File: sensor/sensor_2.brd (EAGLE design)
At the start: 40.1 x 55.9 mm, 29 parts, among them IC1 INA116U, IC3 LT6230LT6010(MOD12.2013), T1 BC849SMD, T2 BC849SMD

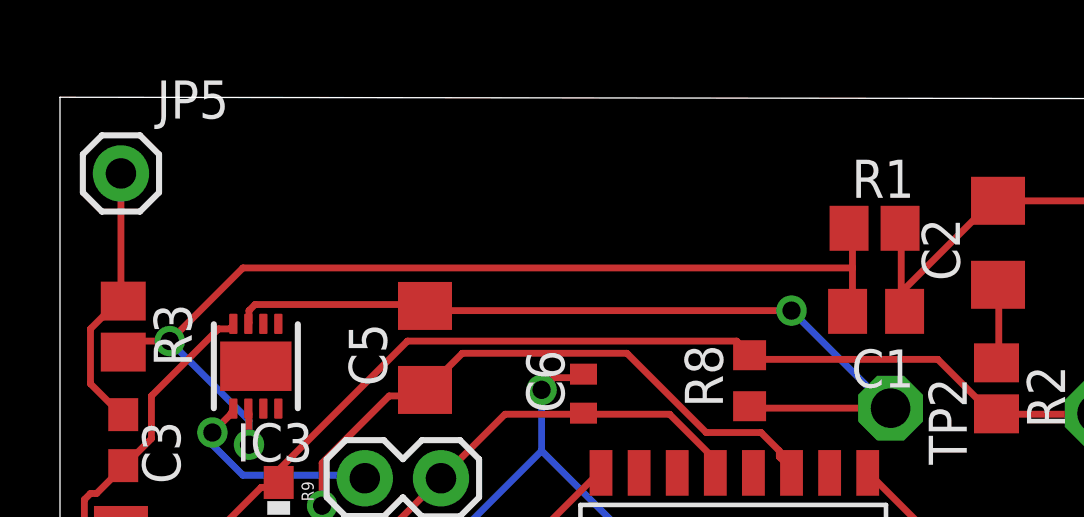
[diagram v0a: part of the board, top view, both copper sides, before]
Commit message: IC3 had green lines that were part of the via layer. Those were removed. There was also a missing trace from PIN2 of the IC3 part. That was restored. Small tweaks were made. Sensor board seems to be done. Next is to export it into the appropriate files for the fre DFM check by Advance Circuits. After that, the board will be submitted to OHSpark.
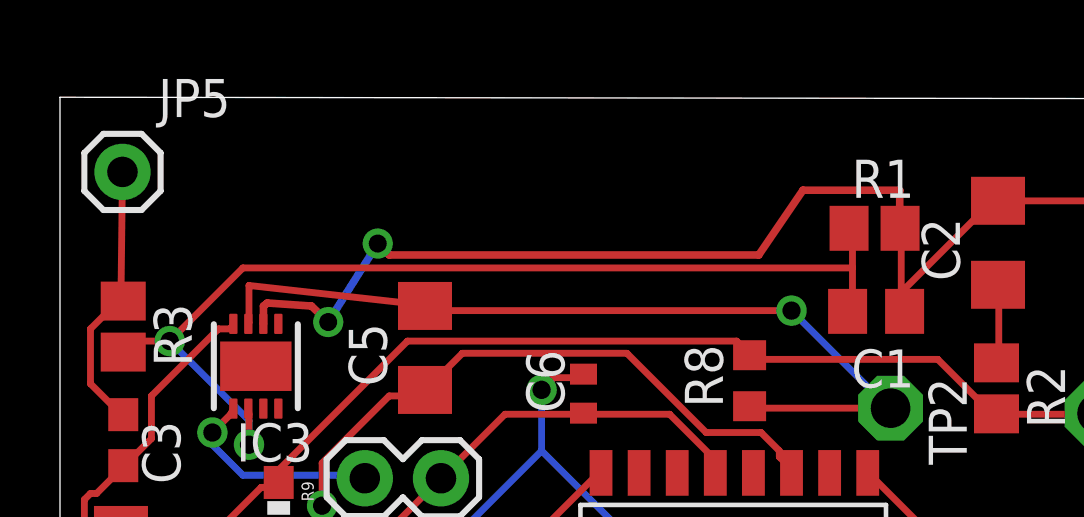
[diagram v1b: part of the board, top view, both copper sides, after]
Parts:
- moved JP5 0.07 mm to (2.08, 53.4)
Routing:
- net N$9: track 12.8 -> 38.9 mm, vias 0 -> 2
- net N$10: track 28.1 -> 28.9 mm
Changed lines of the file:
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@@
 <?xml version="1.0" encoding="utf-8"?>
 <!DOCTYPE eagle SYSTEM "eagle.dtd">
-<eagle version="6.5.0">
+<eagle version="6.4">
 <drawing>
 <settings>
@@
 <element name="JP3" library="SparkFun-Connectors" package="1X02" value="M02PTH" x="12.7" y="43.18" rot="R180"/>
 <element name="JP4" library="SparkFun-Connectors" package="1X02" value="M02PTH" x="10.16" y="38.1" rot="R90"/>
-<element name="JP5" library="SparkFun-Connectors" package="1X01" value="M01PTH" x="2.032" y="53.34"/>
+<element name="JP5" library="SparkFun-Connectors" package="1X01" value="M01PTH" x="2.0828" y="53.3908"/>
 <element name="TP1" library="testpad" package="P1-13" value="TPPAD1-13" x="34.5694" y="45.339" rot="R270">
 <attribute name="TP_SIGNAL_NAME" value="" x="-9.8806" y="-4.191" size="1.778" layer="27" rot="R270" display="off"/>
@@
 <wire x1="2.032" y1="49.1744" x2="1.016" y2="48.1584" width="0.2286" layer="1"/>
 <wire x1="2.032" y1="45.3136" x2="2.1082" y2="45.3" width="0.2286" layer="1"/>
-<wire x1="2.032" y1="53.34" x2="2.032" y2="49.1744" width="0.2286" layer="1"/>
+<wire x1="2.0828" y1="53.3908" x2="2.032" y2="49.1744" width="0.2286" layer="1"/>
 <wire x1="2.032" y1="49.1744" x2="2.1082" y2="49.0846" width="0.2286" layer="1"/>
 </signal>
@@
 <wire x1="31.2928" y1="52.4256" x2="31.2674" y2="52.4286" width="0.2286" layer="1"/>
 <wire x1="35.9664" y1="52.4256" x2="36.0172" y2="52.5272" width="0.2286" layer="1"/>
-<wire x1="6.7778" y1="48.3263" x2="28.0416" y2="48.768" width="0" layer="19" extent="1-1"/>
+<wire x1="6.7778" y1="48.3263" x2="6.7818" y2="48.3263" width="0.254" layer="1"/>
+<wire x1="6.7818" y1="48.3263" x2="6.7818" y2="48.9204" width="0.254" layer="1"/>
+<wire x1="6.9088" y1="49.022" x2="6.8834" y2="48.9966" width="0.254" layer="1"/>
+<wire x1="8.382" y1="48.9204" x2="6.9088" y2="49.022" width="0.254" layer="1"/>
+<wire x1="8.9408" y1="48.387" x2="8.382" y2="48.9204" width="0.254" layer="1"/>
+<wire x1="10.5918" y1="51.0032" x2="8.9408" y2="48.387" width="0.254" layer="16"/>
+<wire x1="10.9728" y1="50.6222" x2="10.5918" y2="51.0032" width="0.254" layer="1"/>
+<wire x1="23.2918" y1="50.6222" x2="10.9728" y2="50.6222" width="0.254" layer="1"/>
+<wire x1="24.765" y1="52.7812" x2="23.2918" y2="50.6222" width="0.254" layer="1"/>
+<wire x1="27.9908" y1="52.7812" x2="24.765" y2="52.7812" width="0.254" layer="1"/>
+<wire x1="27.9908" y1="51.6128" x2="27.9908" y2="52.7812" width="0.254" layer="1"/>
+<wire x1="6.8834" y1="48.9966" x2="6.7818" y2="48.9204" width="0.254" layer="1"/>
+<wire x1="27.9908" y1="51.6128" x2="28.0026" y2="51.5112" width="0.254" layer="1"/>
+<via x="8.9408" y="48.387" extent="1-16" drill="0.6"/>
+<via x="10.5918" y="51.0032" extent="1-16" drill="0.6"/>
 </signal>
 <signal name="N$10">
@@
 <contactref element="IC3" pad="3"/>
 <contactref element="TP2" pad="TP"/>
-<wire x1="6.2992" y1="48.768" x2="6.2992" y2="48.3616" width="0.2286" layer="1"/>
-<wire x1="6.5024" y1="48.9712" x2="6.2992" y2="48.768" width="0.2286" layer="1"/>
-<wire x1="11.9888" y1="48.9712" x2="6.5024" y2="48.9712" width="0.2286" layer="1"/>
+<wire x1="6.2992" y1="49.6062" x2="6.2992" y2="48.3616" width="0.2286" layer="1"/>
+<wire x1="11.9888" y1="48.9712" x2="6.2992" y2="49.6062" width="0.2286" layer="1"/>
 <wire x1="6.2992" y1="48.3616" x2="6.2778" y2="48.3263" width="0.2286" layer="1"/>
 <wire x1="11.9888" y1="48.9712" x2="12.1666" y2="48.9234" width="0.2286" layer="1"/>

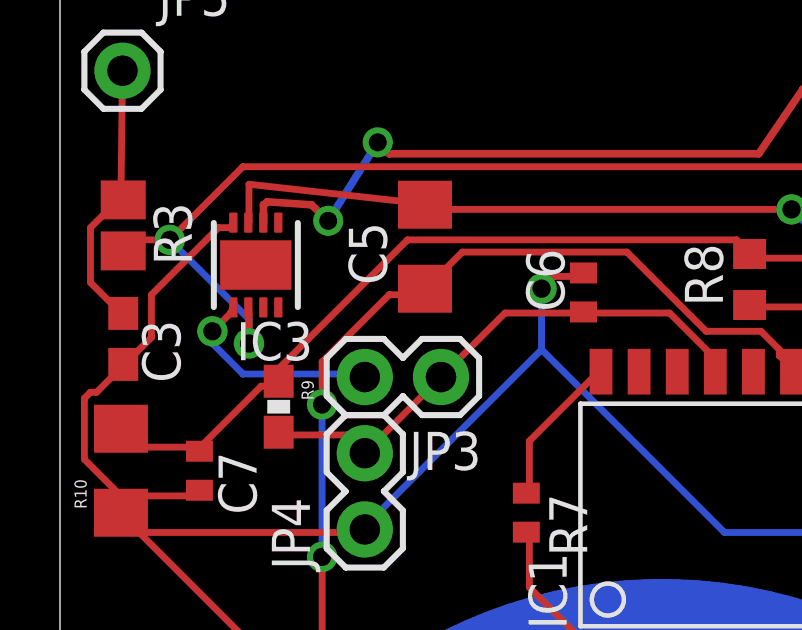
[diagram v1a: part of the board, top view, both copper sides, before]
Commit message: Routed previously missed airwire. Submitting to OHSpark next.
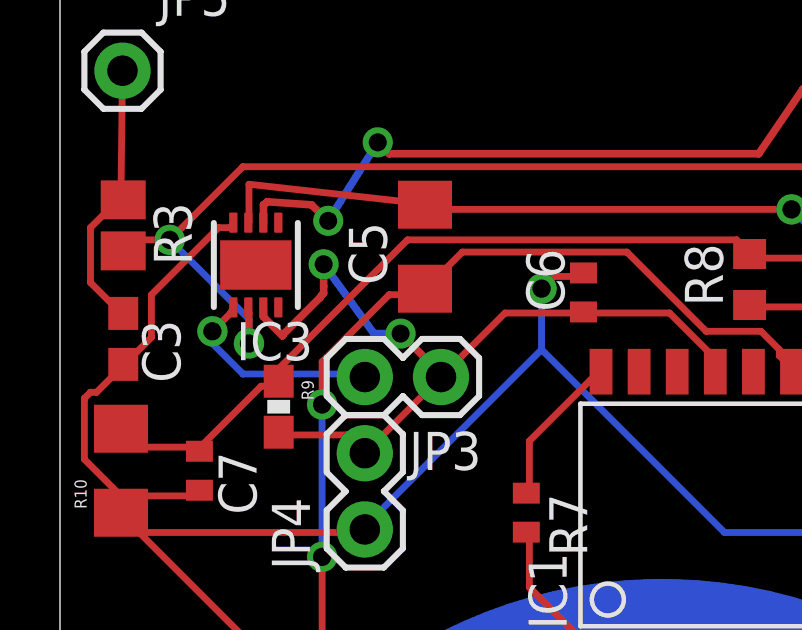
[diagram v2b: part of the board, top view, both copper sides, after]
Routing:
- net 5V: track 17.9 -> 27.8 mm, vias 0 -> 2
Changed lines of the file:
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@@
 <wire x1="17.4752" y1="45.3136" x2="17.4498" y2="45.3494" width="0.2286" layer="1"/>
 <wire x1="12.7" y1="43.18" x2="10.16" y2="40.64" width="0.2286" layer="1"/>
-<wire x1="7.2898" y1="41.3394" x2="6.7778" y2="45.5013" width="0" layer="19" extent="1-1"/>
+<wire x1="6.7778" y1="45.5013" x2="6.7778" y2="45.1906" width="0.254" layer="1"/>
+<wire x1="6.7778" y1="45.1906" x2="7.4168" y2="44.5516" width="0.254" layer="1"/>
+<wire x1="7.4168" y1="44.5516" x2="7.4168" y2="44.577" width="0.254" layer="1"/>
+<wire x1="7.4168" y1="44.577" x2="8.6614" y2="45.8216" width="0.254" layer="1"/>
+<wire x1="8.7884" y1="45.974" x2="8.7884" y2="46.2026" width="0.254" layer="1"/>
+<wire x1="8.7884" y1="46.2026" x2="8.7884" y2="46.6852" width="0.254" layer="1"/>
+<wire x1="8.7376" y1="45.9232" x2="8.7884" y2="45.974" width="0.254" layer="1"/>
+<wire x1="8.7376" y1="45.9232" x2="8.6614" y2="45.8216" width="0.254" layer="1"/>
+<wire x1="11.3538" y1="44.6278" x2="12.6746" y2="43.307" width="0.254" layer="1"/>
+<wire x1="10.4648" y1="44.6278" x2="11.3538" y2="44.6278" width="0.254" layer="16"/>
+<wire x1="8.7884" y1="46.9392" x2="10.4648" y2="44.6278" width="0.254" layer="16"/>
+<wire x1="12.6746" y1="43.307" x2="12.7" y2="43.18" width="0.254" layer="1"/>
+<wire x1="8.7884" y1="46.9392" x2="8.7884" y2="46.6852" width="0.254" layer="1"/>
+<via x="11.3538" y="44.6278" extent="1-16" drill="0.6"/>
+<via x="8.7884" y="46.9392" extent="1-16" drill="0.6"/>
 </signal>
 <signal name="N$4">
